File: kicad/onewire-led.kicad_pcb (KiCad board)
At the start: 2 copper layers, 25.4 x 38.1 mm, 11 parts, among them IC1 ATTINY13A-P, P1 CONN_2

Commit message: Added ground fill to bottom copper
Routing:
- added copper zone on B.Cu, net GND
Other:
- net class Default: clearance 0.508 -> 0.381
- rule trace_clearance: 0.508 -> 0.381
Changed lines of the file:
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@@
   (general
     (links 18)
-    (no_connects 2)
+    (no_connects 0)
     (area 0 0 0 0)
     (thickness 1.6)
@@
   (page A3)
   (layers
-    (15 F.Cu jumper)
+    (15 F.Cu signal)
     (0 B.Cu signal)
     (16 B.Adhes user)
@@
   (setup
     (last_trace_width 0.508)
-    (trace_clearance 0.508)
+    (trace_clearance 0.381)
     (zone_clearance 0.508)
     (zone_45_only no)
@@
   (net 11 VCC)
   (net_class Default "This is the default net class."
-    (clearance 0.508)
+    (clearance 0.381)
     (trace_width 0.508)
     (via_dia 0.889)
@@
   (segment (start 117.094 62.23) (end 113.792 65.532) (width 0.508) (layer F.Cu) (net 5))
   (segment (start 121.412 62.23) (end 117.094 62.23) (width 0.508) (layer F.Cu) (net 5))
-  (segment (start 116.332 57.912) (end 120.65 62.23) (width 0.508) (layer B.Cu) (net 6) (status 400000))
-  (segment (start 120.65 65.024) (end 120.904 65.278) (width 0.508) (layer B.Cu) (net 6) (status C00000))
-  (segment (start 120.65 62.23) (end 120.65 65.024) (width 0.508) (layer B.Cu) (net 6) (status 800000))
+  (segment (start 116.332 57.912) (end 120.65 62.23) (width 0.508) (layer B.Cu) (net 6))
+  (segment (start 120.65 65.024) (end 120.904 65.278) (width 0.508) (layer B.Cu) (net 6))
+  (segment (start 120.65 62.23) (end 120.65 65.024) (width 0.508) (layer B.Cu) (net 6))
   (segment (start 118.364 82.55) (end 118.364 84.582) (width 0.508) (layer B.Cu) (net 7))
   (segment (start 118.364 84.582) (end 115.57 87.376) (width 0.508) (layer B.Cu) (net 7))
@@
   (segment (start 114.3 53.086) (end 113.754 52.54) (width 0.508) (layer B.Cu) (net 11))
   (segment (start 113.754 52.54) (end 112.8 52.54) (width 0.508) (layer B.Cu) (net 11))
+  (zone (net 2) (net_name GND) (layer B.Cu) (hatch edge 0.508)
+    (connect_pads (clearance 0.508))
+    (min_thickness 0.254)
+    (fill (arc_segments 16) (thermal_gap 0.508) (thermal_bridge_width 0.508) (smoothing fillet))
+    (polygon
+      (pts
+        (xy 127 82.55) (xy 123.19 82.55) (xy 116.84 88.9) (xy 111.76 88.9) (xy 105.41 82.55)
+        (xy 101.6 82.55) (xy 101.6 50.8) (xy 127 50.8)
+      )
+    )
+  )
 )

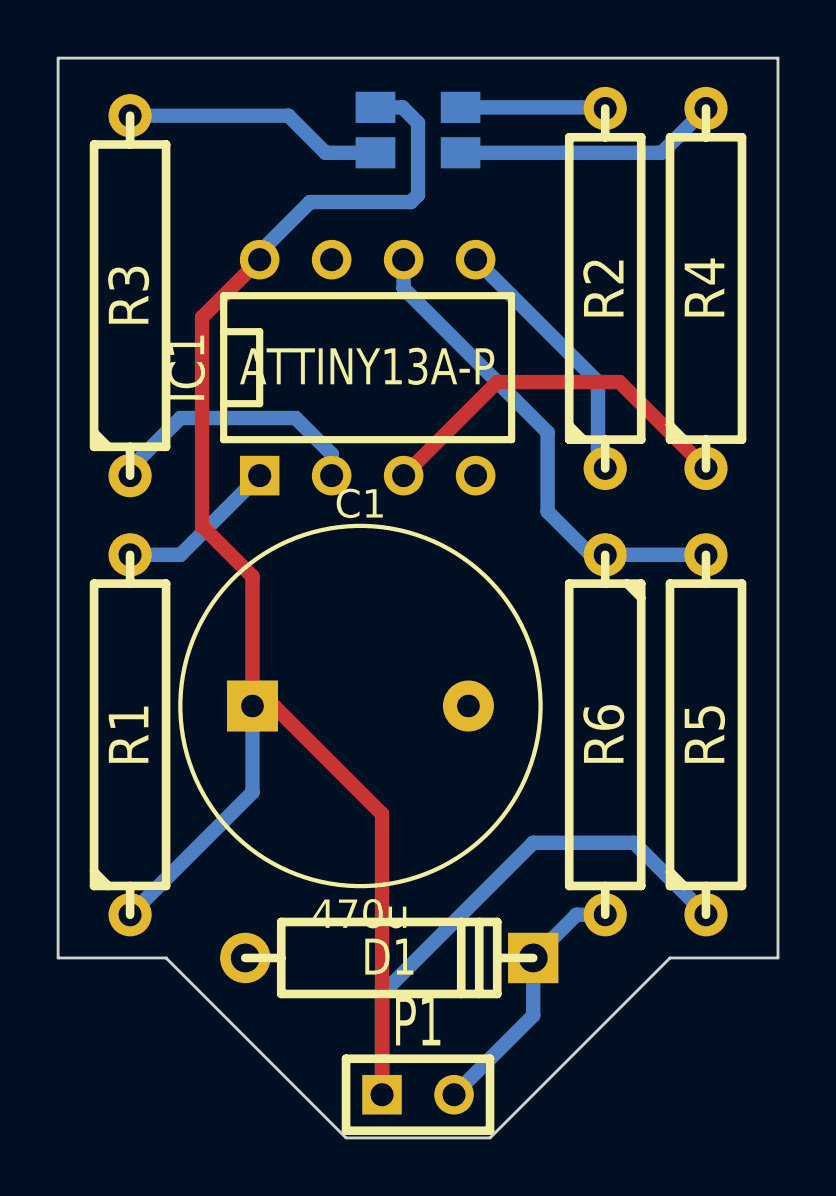
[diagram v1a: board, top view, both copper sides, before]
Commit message: Fixed layout for package sizes and incorrect PLCC layout
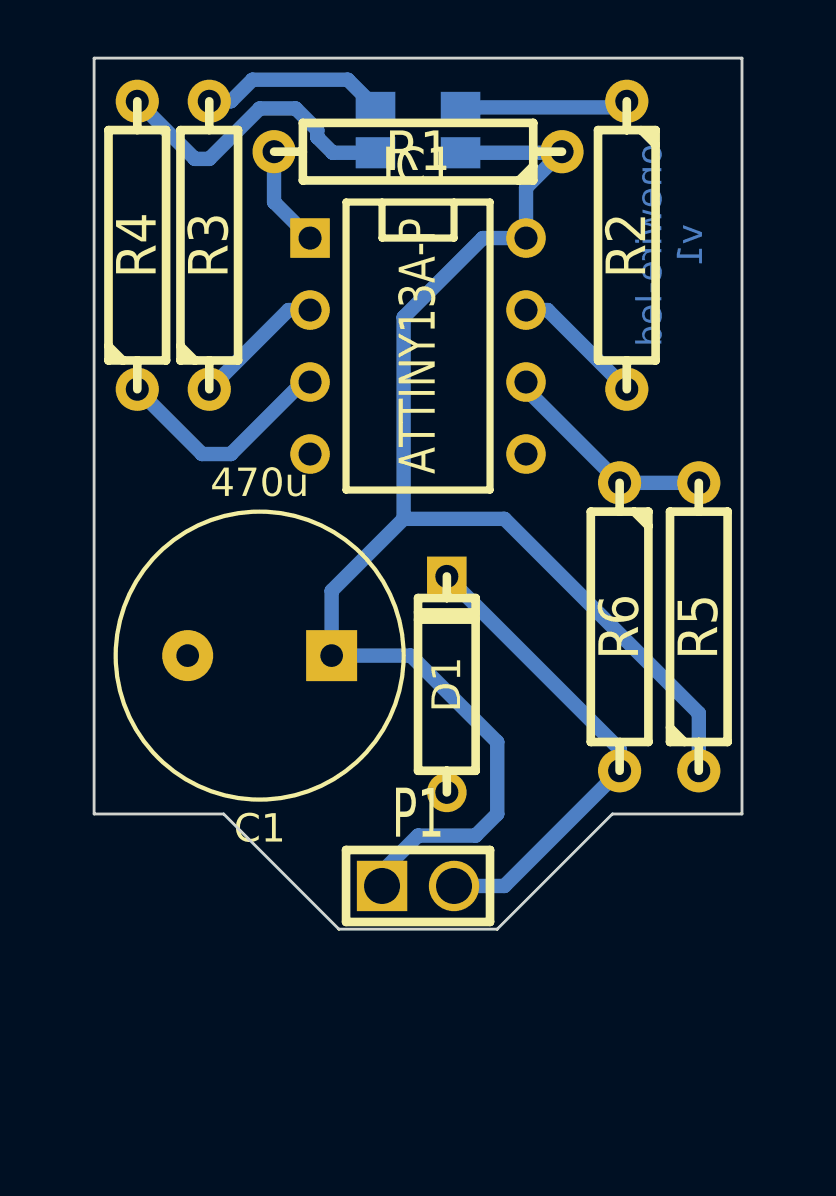
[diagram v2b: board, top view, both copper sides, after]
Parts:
- D1: footprint D4 -> D3
- P1: footprint SIL-2 -> SIL-2-WIDE
- R1, R2, R3, R4, R5, R6: footprint R5 -> R4
- moved R1 22.9 mm to (114.3, 54.1), turned to 180 degrees
- moved R4 20.1 mm to (104.4, 57.4)
- moved D1 9.86 mm to (115.3, 72.9), turned to 90 degrees
- moved P1 7.37 mm to (114.3, 80.0)
- moved C1 3.98 mm to (108.7, 71.9), turned to 180 degrees
- moved R6 3.84 mm to (121.4, 70.9)
- moved R5 3.82 mm to (124.2, 70.9)
- moved R3 3.31 mm to (106.9, 57.4)
- moved IC1 1.93 mm to (114.3, 61.0), turned to 270 degrees
- moved R2 1.70 mm to (121.7, 57.4), turned to 270 degrees
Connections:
- IC1 pad 2: N-000001 (its old number) -> /green
- IC1 pad 3: N-0000011 (its old number) -> /blue
- IC1 pad 5: N-000002 -> (no net)
- IC1 pad 7: (no net) -> /red
- LED1 pad 1: N-000009 -> N-000004
- R2 pad 1: N-000002 -> N-000004
- R2 pad 2: N-000009 -> /red
- R3 pad 1: N-000001 (its old number) -> /green
- R4 pad 1: N-0000011 (its old number) -> /blue
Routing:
- net VCC: track 71.7 -> 56.0 mm
- net N-0000011 (its old number): track 13.3 -> 0.00 mm
- net /Vsense: track 17.2 -> 7.72 mm
- net N-000001 (its old number): track 9.39 -> 0.00 mm
- net N-000002: track 9.26 -> 0.00 mm
- net /blue: track 0.00 -> 8.09 mm
- net N-0000011: track 9.15 -> 16.9 mm
- net N-000004: track 0.00 -> 5.96 mm
- net N-000009: track 5.12 -> 0.00 mm
- net /red: track 0.00 -> 4.71 mm
- net /green: track 0.00 -> 4.71 mm
- net N-000005: track 9.20 -> 6.59 mm
- net N-000003: track 5.73 -> 3.57 mm
- net N-000001: track 9.31 -> 10.8 mm
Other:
- board size 25.4 x 38.1 mm -> 22.9 x 30.7 mm
- board text added: "onewire-led v1"
